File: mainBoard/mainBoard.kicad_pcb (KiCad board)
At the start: 4 copper layers, 300 x 247.4 mm, 260 parts, among them J1 1366005, J10 Conn_01x02, J11 Conn_02x05_Odd_Even, J12 Conn_01x02, J13 Conn_01x02, J14 Conn_01x06, J15 Conn_01x04, J16 Conn_01x07, J17 Conn_01x05, J18 Conn_01x04, J2 USB_A, J3 1714971, J4 1714971, J5 4DB-P108-02, J6 4DB-P108-02, J7 4DB-P108-02, J8 Conn_01x02, J9 Conn_01x02, K1 Relay_SPDT, Q1 IRLML6244TRPBF, Q2 IRLML6244TRPBF, Q3 IRLML6244TRPBF, Q4 IRLML6244TRPBF, Q5 IRLML6244TRPBF, Q6 IRLML6244TRPBF, Q7 IRLML6244TRPBF, SW1 SW_SPST, SW2 SW_SPDT, SW3 SW_Push, SW4 SW_Push, U1 RT6255BHGJ8F, U10 DS18B20+, U11 OPA333AIDCKT, U12 OPA333AIDCKT, U13 DS18B20+, U14 DS18B20+, U15 OPA333AIDCKT, U16 DS18B20+, U17 SFH617A-2, U18 USBLC6-4SC6, U19 USBLC6-4SC6, U2 RT9059GSP, U20 USBLC6-4SC6, U21 USBLC6-4SC6, U22 100, U23 USBLC6-4SC6, U24 USBLC6-2SC6, U25 100, U26 100, U3 RT9059GSP, U4 TPS2041B, U5 USBLC6-2SC6, U6 STM32F401RETx, U7 MOC3083S-TA1, U8 MOC3083S-TA1, U9 DS18B20+, Y1 ATS240C-E

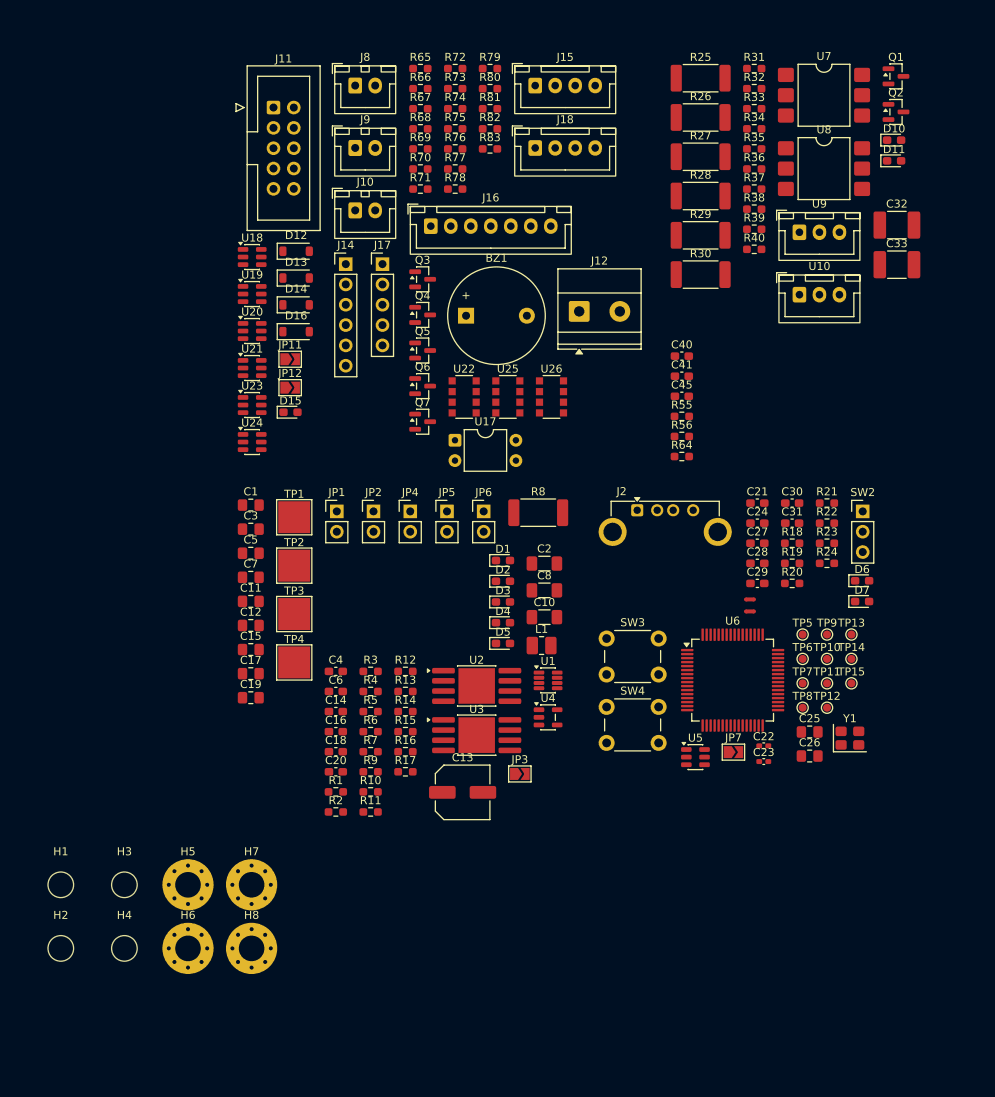
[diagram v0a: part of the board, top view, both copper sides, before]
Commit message: recreated a bunch of parts on the pcb layout
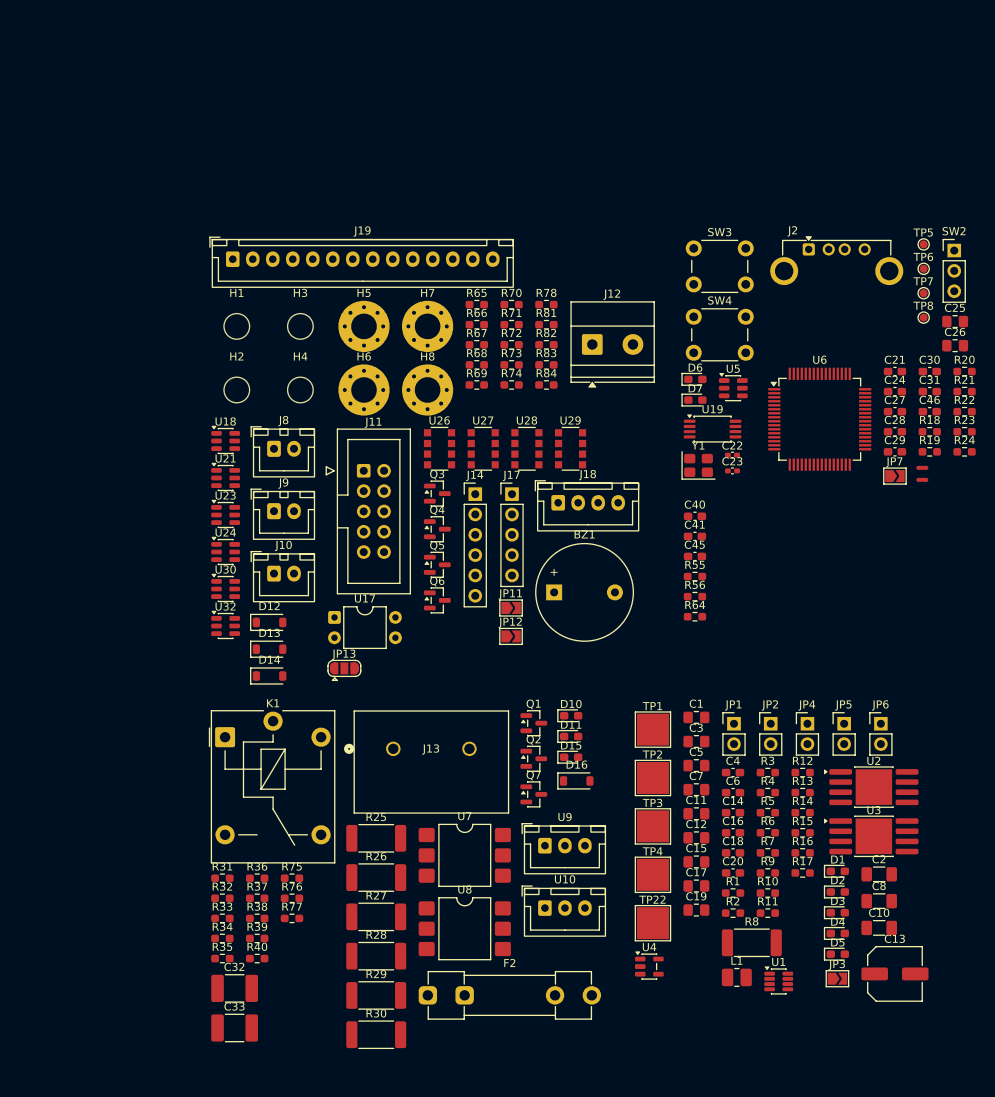
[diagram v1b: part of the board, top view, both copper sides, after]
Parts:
- removed J15: Conn_01x04, Connector_JST:JST_XH_B4B-XH-A_1x04_P2.50mm_Vertical
- removed J16: Conn_01x07, Connector_JST:JST_XH_B7B-XH-A_1x07_P2.50mm_Vertical
- removed R79, R80: 4.7k, Resistor_SMD:R_0603_1608Metric_Pad0.98x0.95mm_HandSolder
- removed TP10, TP11, TP12, TP13, TP14, TP15, TP9: TestPoint_Small, TestPoint:TestPoint_Pad_D1.0mm
- removed U20: USBLC6-4SC6, Package_TO_SOT_SMD:SOT-23-6
- removed U22, U25: 100, Resistor_SMD:R_Array_Convex_4x1206
- added C46: 100nF, Capacitor_SMD:C_0603_1608Metric_Pad1.08x0.95mm_HandSolder, F.Cu at (540.1, 52.9)
- added F2: 3A, Fuse:Fuseholder_Clip-5x20mm_Littelfuse_100_Inline_P20.50x4.60mm_D1.30mm_Horizontal, F.Cu at (477.4, 125.9)
- added J13: Conn_01x02, PhoenixContact_MKDS_9mm:CONN_1714971_PXC, F.Cu at (473.0, 95.1)
- added J19: Conn_01x14, Connector_JST:JST_XH_B14B-XH-A_1x14_P2.50mm_Vertical, F.Cu at (453.0, 33.9)
- added JP13: Jumper_3_Open, Jumper:SolderJumper-3_P1.3mm_Open_RoundedPad1.0x1.5mm, F.Cu at (466.9, 85.0)
- added K1: Relay_SPDT, Relay_THT:Relay_SPDT_Finder_36.11, F.Cu at (452.0, 93.6)
- added R84: 10k, Resistor_SMD:R_0603_1608Metric_Pad0.98x0.95mm_HandSolder, F.Cu at (492.2, 49.6)
- added TP22: TestPoint, TestPoint:TestPoint_Pad_4.0x4.0mm, F.Cu at (505.5, 116.9)
- added U27: 100, Resistor_SMD:R_Array_Convex_4x1206, F.Cu at (484.3, 57.6)
- added U28: 100, Resistor_SMD:R_Array_Convex_4x1206, F.Cu at (489.7, 57.6)
- added U29: 100, Resistor_SMD:R_Array_Convex_4x1206, F.Cu at (495.2, 57.6)
- added U30: 74LVC1T45W6-7, Package_TO_SOT_SMD:SOT-23-6, F.Cu at (452.1, 75.1)
- added U32: 74LVC1T45W6-7, Package_TO_SOT_SMD:SOT-23-6, F.Cu at (452.1, 79.7)
- U19: value USBLC6-4SC6 -> 23LC1024-I/ST; footprint Package_TO_SOT_SMD:SOT-23-6 -> Package_SO:TSSOP-8_4.4x3mm_P0.65mm
- U6: value STM32F401RETx -> STM32F413RHT6
- moved C32 126.3 mm to (453.2, 125.0)
- moved C33 126.3 mm to (453.2, 130.0)
- moved R33 121.1 mm to (451.7, 116.3)
- moved R31 121.1 mm to (451.7, 111.3)
- moved R32 121.1 mm to (451.7, 113.8)
- moved R34 121.1 mm to (451.7, 118.8)
- moved R35 121.1 mm to (451.7, 121.3)
- moved R36 108.3 mm to (456.0, 111.3)
- moved R37 108.3 mm to (456.0, 113.8)
- moved R38 108.3 mm to (456.0, 116.3)
- moved R39 108.3 mm to (456.0, 118.8)
- moved R40 108.3 mm to (456.0, 121.3)
- moved U7 105.1 mm to (482.0, 108.4)
- moved U8 105.1 mm to (482.0, 117.6)
- moved R25 103.3 mm to (470.9, 106.3)
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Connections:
- net /Project Architecture/Peripherals and Connectors/CONVFAN_FET_G renamed /Project Architecture/TRIAC/CONVFAN_FET_G
- net /Project Architecture/Peripherals and Connectors/D15_K renamed /Project Architecture/TRIAC/D15_K
- D16 pad 2: /Project Architecture/Peripherals and Connectors/CONVFAN_RELAY_MINUS -> /Project Architecture/TRIAC/CONVFAN_RELAY_MINUS
- D6 pad 2: /Project Architecture/MCU/STM_USR_LED1 -> STM_USR_LED1
- J18 pad 3: +3.3V -> /Project Architecture/Peripherals and Connectors/SOF_PWR_ESD
- J18 pad 4: /Project Architecture/Peripherals and Connectors/SOF_PWR_ESD -> +3.3V
- Q7 pad 3: /Project Architecture/Peripherals and Connectors/CONVFAN_RELAY_MINUS -> /Project Architecture/TRIAC/CONVFAN_RELAY_MINUS
- R20 pad 2: /Project Architecture/MCU/STM_USR_BTN -> STM_USR_BTN
- R75 pad 2: /Project Architecture/Peripherals and Connectors/CONVFAN_RELAY_MINUS -> /Project Architecture/TRIAC/CONVFAN_RELAY_MINUS
- SW4 pad 1: /Project Architecture/MCU/STM_USR_BTN -> STM_USR_BTN
- U19 pad 1: /Project Architecture/Peripherals and Connectors/KP_ESD_R30 -> QSPI_SRAM_CS
- U19 pad 2: GND -> QSPI_SIO1
- U19 pad 3: /Project Architecture/Peripherals and Connectors/KP_ESD_R1 -> QSPI_SIO2
- U19 pad 4: /Project Architecture/Peripherals and Connectors/KP_ESD_R2 -> GND
- U19 pad 5: +3.3V -> QSPI_SIO0
- U19 pad 6: /Project Architecture/Peripherals and Connectors/KP_ESD_R3 -> QSPI_SCK
- U6 pad 10: Fan2 -> unconnected-(U6-PC2-Pad10)
- U6 pad 11: Fan3 -> unconnected-(U6-PC3-Pad11)
- U6 pad 14: /Project Architecture/MCU/STM_USR_BTN -> unconnected-(U6-PA0-Pad14)
- U6 pad 15: Soft_Power -> QSPI_SIO3
- U6 pad 16: TC2_ADC -> unconnected-(U6-PA2-Pad16)
- U6 pad 17: TC2_CJ_TEMP -> unconnected-(U6-PA3-Pad17)
- U6 pad 2: DOOR_SW -> unconnected-(U6-PC13-Pad2)
- U6 pad 20: TC3_ADC -> unconnected-(U6-PA4-Pad20)
- U6 pad 21: USB_OC -> unconnected-(U6-PA5-Pad21)
- U6 pad 22: TC3_CJ_TEMP -> TC1_ADC
- U6 pad 23: TC1_ADC -> TC2_ADC
- U6 pad 24: TC1_CJ_TEMP -> unconnected-(U6-PC4-Pad24)
- U6 pad 25: Net-(U6-PC5) -> unconnected-(U6-PC5-Pad25)
- U6 pad 26: Net-(U6-PB0) -> TC3_ADC
- U6 pad 27: Net-(U6-PB1) -> QSPI_SCK
- U6 pad 28: Net-(U6-PB2) -> unconnected-(U6-PB2-Pad28)
- U6 pad 29: Net-(U6-PB10) -> unconnected-(U6-PB10-Pad29)
- U6 pad 3: Net-(U6-PC14) -> unconnected-(U6-PC14-Pad3)
- U6 pad 33: PB12 -> unconnected-(U6-PB12-Pad33)
- U6 pad 34: PB13 -> unconnected-(U6-PB13-Pad34)
- U6 pad 35: PB14 -> unconnected-(U6-PB14-Pad35)
- U6 pad 36: PB15 -> unconnected-(U6-PB15-Pad36)
- U6 pad 37: PC6 -> unconnected-(U6-PC6-Pad37)
- U6 pad 38: Bottom_Heater -> unconnected-(U6-PC7-Pad38)
- U6 pad 39: TRIAC_BOT_TEMP -> QSPI_SIO2
- U6 pad 4: Net-(U6-PC15) -> unconnected-(U6-PC15-Pad4)
- U6 pad 40: Top_Heater -> QSPI_SIO0
- U6 pad 41: TRIAC_TOP_TEMP -> unconnected-(U6-PA8-Pad41)
- U6 pad 43: USB_EN -> unconnected-(U6-PA10-Pad43)
- U6 pad 50: /Project Architecture/MCU/STM_USR_LED1 -> unconnected-(U6-PA15-Pad50)
- U6 pad 51: STM_USR_LED2 -> QSPI_SIO1
- U6 pad 52: KP_Col0 -> unconnected-(U6-PC11-Pad52)
- U6 pad 53: KP_Col1 -> unconnected-(U6-PC12-Pad53)
- U6 pad 54: KP_Col2 -> unconnected-(U6-PD2-Pad54)
- U6 pad 55: KP_Row0 -> SPI1_SCK
- U6 pad 56: KP_Row1 -> SPI1_MISO
- U6 pad 57: KP_Row2 -> SPI1_MOSI
- U6 pad 58: KP_Row3 -> QSPI_SRAM_CS
- U6 pad 59: Buzzer -> unconnected-(U6-PB7-Pad59)
- U6 pad 61: I2C_CLK -> unconnected-(U6-PB8-Pad61)
- U6 pad 62: I2C_SDA -> unconnected-(U6-PB9-Pad62)
- U6 pad 8: Conv_Fan -> unconnected-(U6-PC0-Pad8)
- U6 pad 9: Fan1 -> unconnected-(U6-PC1-Pad9)

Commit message: replace piezo with actual speaker
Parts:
- removed BZ1: Buzzer, Buzzer_Beeper:Buzzer_12x9.5RM7.6
- removed Q6: IRLML6244TRPBF, Package_TO_SOT_SMD:SOT-23
- removed R68: 220, Resistor_SMD:R_0603_1608Metric_Pad0.98x0.95mm_HandSolder
- removed R72: 10k, Resistor_SMD:R_0603_1608Metric_Pad0.98x0.95mm_HandSolder
- removed R73: 1k, Resistor_SMD:R_0603_1608Metric_Pad0.98x0.95mm_HandSolder
- added C47: 100uF, Capacitor_SMD:C_Elec_6.3x5.8, F.Cu at (593.8, 85.2)
- added C48: 100uF, Capacitor_SMD:C_Elec_6.3x5.8, F.Cu at (593.8, 93.4)
- added C49: 100nF, Capacitor_SMD:C_0805_2012Metric_Pad1.18x1.45mm_HandSolder, F.Cu at (610.6, 82.7)
- added C50: 10uF, Capacitor_SMD:C_0805_2012Metric_Pad1.18x1.45mm_HandSolder, F.Cu at (610.6, 85.7)
- added C51: 100nF, Capacitor_SMD:C_0805_2012Metric_Pad1.18x1.45mm_HandSolder, F.Cu at (610.6, 88.7)
- added C52: 1uF, Capacitor_SMD:C_0805_2012Metric_Pad1.18x1.45mm_HandSolder, F.Cu at (610.6, 91.7)
- added C53: 10nF, Capacitor_SMD:C_0603_1608Metric_Pad1.08x0.95mm_HandSolder, F.Cu at (615.1, 85.4)
- added LS1: Speaker, Connector_JST:JST_PH_B2B-PH-K_1x02_P2.00mm_Vertical, F.Cu at (647.1, 102.2)
- added R79: 10, Resistor_SMD:R_0603_1608Metric_Pad0.98x0.95mm_HandSolder, F.Cu at (596.0, 67.3)
- added R80: TC33X-2-102E, Potentiometer_SMD:Potentiometer_Bourns_TC33X_Vertical, F.Cu at (566.0, 100.2)
- added R85: 2.2k, Resistor_SMD:R_0603_1608Metric_Pad0.98x0.95mm_HandSolder, F.Cu at (615.1, 87.9)
- added U20: LM386, Package_SO:SOIC-8_3.9x4.9mm_P1.27mm, F.Cu at (610.3, 77.8)
- C22, C23: value 20pF -> 16pF
- Y1: value ATS240C-E -> RH100-48.000-10-F-1015-X-TR-NS1
- moved C34 110.1 mm to (272.2, 54.0)
- moved C35 110.1 mm to (302.3, 54.3)
- moved R41 110.1 mm to (275.8, 54.0)
- moved R42 110.1 mm to (305.9, 54.3)
- moved R43 110.1 mm to (268.6, 54.0)
- moved R44 110.1 mm to (298.7, 54.3)
- moved U13 110.1 mm to (260.1, 47.5)
- moved U14 110.1 mm to (290.2, 47.9)
- moved C36 110.1 mm to (271.7, 64.5)
- moved C37 110.1 mm to (301.8, 64.8)
- moved C38 110.1 mm to (277.7, 64.0)
- moved C39 110.1 mm to (307.8, 64.3)
- moved C42 110.1 mm to (331.0, 53.6)
- moved C43 110.1 mm to (330.5, 64.1)
- moved C44 110.1 mm to (336.6, 63.6)
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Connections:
- Y1 pad 2: /Project Architecture/MCU/HSE_IN -> GND
- Y1 pad 3: (no net) -> /Project Architecture/MCU/HSE_IN
- Y1 pad 4: (no net) -> GND

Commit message: working on layout
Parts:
- removed the F2 at (473.2, 131.5)
- removed the J13 at (468.8, 100.7)
- removed the K1 at (192.0, -29.3)
- removed TP1, TP2: TestPoint, TestPoint:TestPoint_Pad_4.0x4.0mm
- added C54: 22uF, Capacitor_SMD:C_1206_3216Metric_Pad1.33x1.80mm_HandSolder, F.Cu at (235.5, 145.1)
- added D17: GRN, LED_SMD:LED_0603_1608Metric_Pad1.05x0.95mm_HandSolder, F.Cu at (298.6, 105.9)
- added H10: MountingHole_Pad, MountingHole:MountingHole_3.2mm_M3_Pad_Via, F.Cu at (314.0, 199.6)
- added H9: MountingHole_Pad, MountingHole:MountingHole_3.2mm_M3_Pad_Via, F.Cu at (350.4, 199.6)
- added TP10: TestPoint_Small, TestPoint:TestPoint_Pad_D1.0mm, F.Cu at (262.3, 96.5)
- added TP9: TestPoint_Small, TestPoint:TestPoint_Pad_D1.0mm, F.Cu at (283.2, 106.8)
- added kobee-studio-6A788950: Kobee Studio, kobee-studio-6A788950, F.Cu at (338.6, 166.1)
- added kobee-studio-6A78A34B: Kobee Studio, kobee-studio-6A788922, F.Cu at (269.5, 157.6)
- added kobee-studio-6A78A548: Kobee Studio, kobee-studio-6A78A4EC, F.Cu at (283.7, 178.9)
- added kobee-studio-6A78A618: Kobee Studio, kobee-studio-6A78A618, F.Cu at (266.2, 162.1)
- added kobee-studio-6A78A6FA: Kobee Studio, kobee-studio-6A78A483, F.Cu at (269.3, 146.4)
- added kobee-studio-6A78A703: Kobee Studio, kobee-studio-6A78A5D5, F.Cu at (266.1, 151.0)
- added kobee-studio-6A78B988: Kobee Studio, kobee-studio-6A78B988, F.Cu at (213.0, 150.9)
- added kobee-studio-6A78B9B1: Kobee Studio, kobee-studio-6A78B9B1, F.Cu at (207.1, 145.6)
- added kobee-studio-6A7920CC: Kobee Studio, kobee-studio-6A7920CC, F.Cu at (287.6, 94.2)
- added kobee-studio-6A79213B: Kobee Studio, kobee-studio-6A791FA5, F.Cu at (342.1, 182.5)
- added kobee-studio-6A79225D: Kobee Studio, kobee-studio-6A791EC5, F.Cu at (319.3, 176.1)
- C4: footprint Capacitor_SMD:C_0603_1608Metric_Pad1.08x0.95mm_HandSolder -> Capacitor_SMD:C_0402_1005Metric_Pad0.74x0.62mm_HandSolder
- JP3: moved to B.Cu
- TP22: footprint TestPoint:TestPoint_Pad_4.0x4.0mm -> TestPoint:TestPoint_Pad_D2.0mm
- moved H7 411.6 mm to (82.8, 179.0)
- moved R71 409.8 mm to (94.7, 174.7), turned to 90 degrees
- moved R65 407.1 mm to (94.7, 179.0), turned to 90 degrees
- moved R66 403.9 mm to (97.2, 179.0), turned to 90 degrees
- moved R67 400.7 mm to (99.7, 179.0), turned to 90 degrees
- moved Q3 400.2 mm to (107.4, 174.4), turned to 90 degrees
- moved R69 397.5 mm to (102.2, 179.0), turned to 90 degrees
- moved Q4 394.7 mm to (111.9, 174.4), turned to 90 degrees
- moved R70 394.4 mm to (104.7, 179.0), turned to 90 degrees
- moved Q5 389.3 mm to (116.3, 174.4), turned to 90 degrees
- moved D15 389.0 mm to (103.6, 136.1)
- moved D16 389.0 mm to (104.3, 139.1)
- moved Q7 389.0 mm to (98.9, 140.8)
- moved J8 376.6 mm to (90.5, 162.7)
- moved D12 368.5 mm to (122.8, 177.6), turned to 90 degrees
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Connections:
- net Net-(JP1-A) renamed /Project Architecture/Power Supply/+3v3_Vout
- F2 pad 1: /Project Architecture/Peripherals and Connectors/CONVFAN_L1_FUSED -> /Project Architecture/TRIAC/CONVFAN_L1_FUSED
- F2 pad 2: /Project Architecture/Peripherals and Connectors/CONVFAN_L1 -> /Project Architecture/TRIAC/CONVFAN_L1
- J1 pad 1: L1-120VAC -> LN
- J1 pad 3: LN -> L1-120VAC
- J13 pad 1: /Project Architecture/Peripherals and Connectors/CONVFAN_L1 -> /Project Architecture/TRIAC/CONVFAN_L1
- J13 pad 2: /Project Architecture/Peripherals and Connectors/CONVFAN_L1_SW -> /Project Architecture/TRIAC/CONVFAN_L1_SW
- U5 pad 1: Net-(J2-D+) -> Net-(J2-D-)
- U5 pad 3: Net-(J2-D-) -> Net-(J2-D+)
- U5 pad 4: USB_DN -> USB_DP
- U5 pad 6: USB_DP -> USB_DN
- U7 pad 4: /Project Architecture/TRIAC/L1_F2_OPTO_TOP -> /Project Architecture/TRIAC/L1_OPTO_TOP
- U7 pad 6: /Project Architecture/TRIAC/L1_OPTO_TOP -> /Project Architecture/TRIAC/L1_F2_OPTO_TOP
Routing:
- net LN: track 0.00 -> 77.9 mm
- net SWDCLK: track 0.00 -> 55.8 mm
- net SWDIO: track 0.00 -> 55.3 mm
- net USB_DP: track 0.00 -> 51.6 mm
- net USB_DN: track 0.00 -> 51.2 mm
- net VBUS: track 0.00 -> 39.5 mm
- net Net-(C47-Pad1): track 0.00 -> 22.4 mm
- net Net-(JP2-A): track 0.00 -> 15.8 mm
- net /Project Architecture/Power Supply/+3v3_Vout: track 0.00 -> 15.6 mm
- net +5V: track 0.00 -> 11.4 mm
- net Net-(JP4-B): track 0.00 -> 10.1 mm
- net NRST_SW: track 0.00 -> 8.32 mm
- net Net-(C47-Pad2): track 0.00 -> 7.89 mm
- net Net-(C6-Pad2): track 0.00 -> 7.69 mm
- net Net-(U20-+): track 0.00 -> 6.98 mm
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- added copper zone on F.Cu, net +12V
- added copper zone on F.Cu, net +5V
- added copper zone on F.Cu, net /Project Architecture/Power Supply/+3v3_Vout
- added copper zone on F.Cu, net /Project Architecture/Power Supply/AC_DC_+12V
- added copper zone on F.Cu, net GND
- added copper zone on F.Cu, net Net-(JP2-A)
- added copper zone on F.Cu, net Net-(U1-LX)
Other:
- board size 300 x 247.4 mm -> 274.8 x 239.2 mm
- board text added: "D+"
- board text added: "D-"
